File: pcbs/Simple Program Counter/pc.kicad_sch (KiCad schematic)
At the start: 18 parts, among them U201 74HCT574, U202 74HC245, U203 74HC14

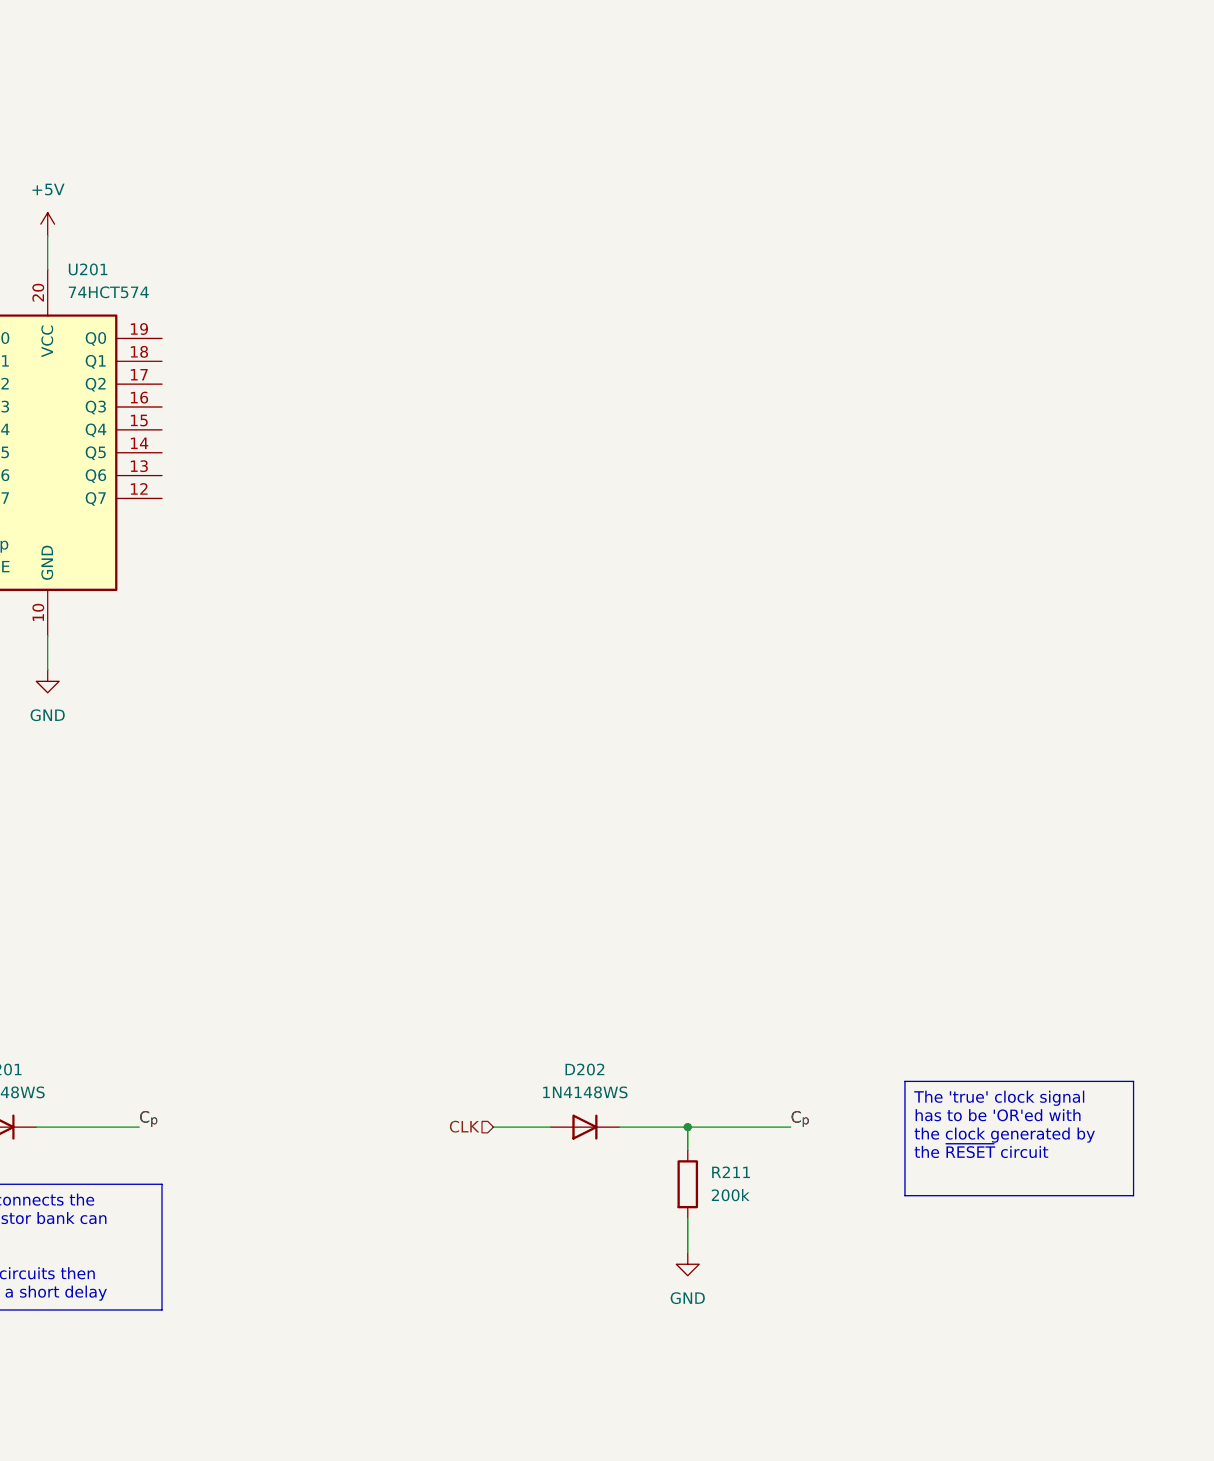
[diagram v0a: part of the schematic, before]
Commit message: Adding indicator LEDs
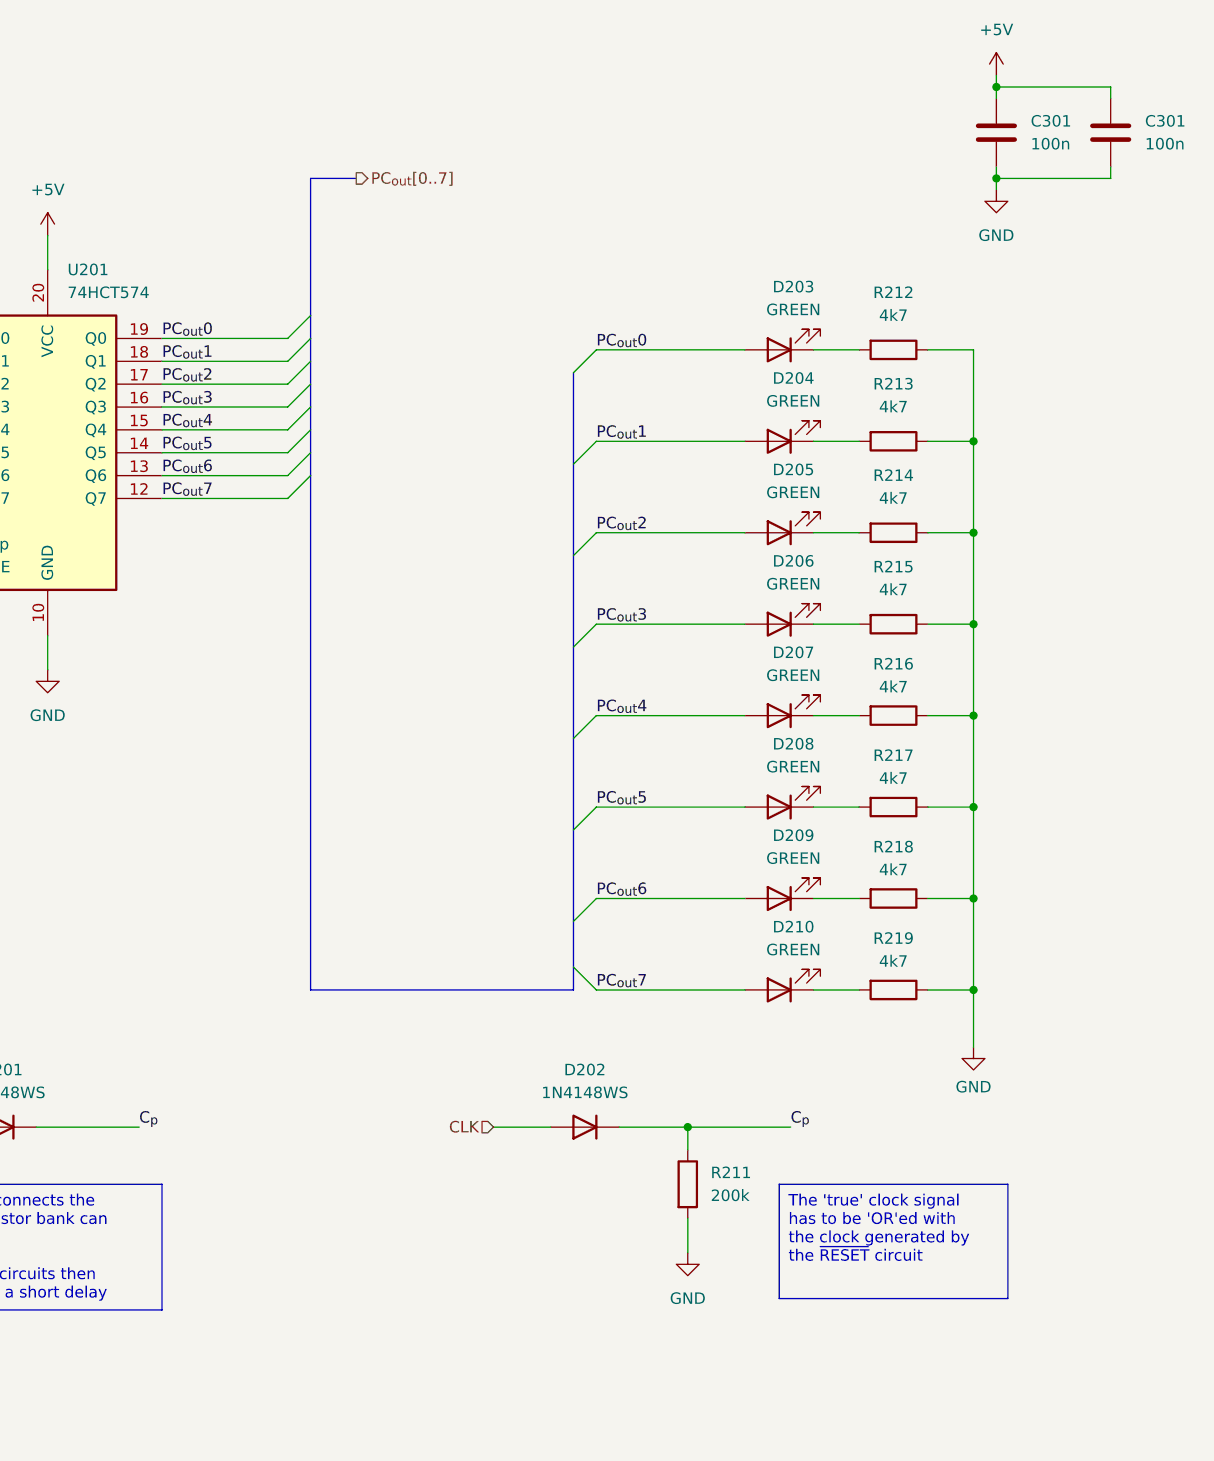
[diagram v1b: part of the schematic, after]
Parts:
- added C301 (x2): 100n, Capacitor_SMD:C_0603_1608Metric, symbol Device:C
- added D203, D204, D205, D206, D207, D208, D209, D210: GREEN, LED_SMD:LED_0603_1608Metric, symbol Device:LED
- added R212, R213, R214, R215, R216, R217, R218, R219: 4k7, Resistor_SMD:R_0603_1608Metric, symbol Device:R
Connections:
- net +5V: now also C301.1, C301.1
- net GND: now also C301.2, C301.2, R212.1, R213.1, R214.1, R215.1, R216.1, R217.1, R218.1, R219.1
- net PC_{out}7: now reaches U201.12 (Q7)
- net PC_{out}7: now also D210.2 (A)
- net PC_{out}6: now reaches U201.13 (Q6)
- net PC_{out}6: now also D209.2 (A)
- net PC_{out}5: now reaches U201.14 (Q5)
- net PC_{out}5: now also D208.2 (A)
- net PC_{out}4: now reaches U201.15 (Q4)
- net PC_{out}4: now also D207.2 (A)
- net PC_{out}3: now reaches U201.16 (Q3)
- net PC_{out}3: now also D206.2 (A)
- net PC_{out}2: now reaches U201.17 (Q2)
- net PC_{out}2: now also D205.2 (A)
- net PC_{out}1: now reaches U201.18 (Q1)
- net PC_{out}1: now also D204.2 (A)
- net PC_{out}0: now reaches U201.19 (Q0)
- net PC_{out}0: now also D203.2 (A)
- new net: D203.1 (K), R212.2
- new net: D209.1 (K), R218.2
- new net: D204.1 (K), R213.2
- new net: D205.1 (K), R214.2
- new net: D207.1 (K), R216.2
- new net: D210.1 (K), R219.2
- new net: D206.1 (K), R215.2
- new net: D208.1 (K), R217.2
